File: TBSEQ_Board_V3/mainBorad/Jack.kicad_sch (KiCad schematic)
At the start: 7 parts

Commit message: BoardV3
ERCチェック済
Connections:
- net D+PlugIn_SyncIn: no longer names the net of DgJ9.4 (3)
- no-connect marks 3 -> 4
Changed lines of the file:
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@@
 		(at 97.79 66.04)
 	)
-	(wire
-		(pts
-			(xy 92.71 124.46) (xy 92.71 118.11)
-		)
-		(stroke
-			(width 0)
-			(type default)
-		)
+	(no_connect
+		(at 96.52 118.11)
 	)
 	(wire
@@
 		(pts
 			(xy 128.27 118.11) (xy 119.38 118.11)
-		)
-		(stroke
-			(width 0)
-			(type default)
-		)
-	)
-	(wire
-		(pts
-			(xy 96.52 124.46) (xy 92.71 124.46)
-		)
-		(stroke
-			(width 0)
-			(type default)
-		)
-	)
-	(wire
-		(pts
-			(xy 92.71 118.11) (xy 96.52 118.11)
 		)
 		(stroke
@@
 				(hide yes)
 			)
-		)
-	)
-	(global_label "D+PlugIn_SyncIn"
-		(shape output)
-		(at 96.52 124.46 0)
-		(fields_autoplaced yes)
-		(effects
-			(font
-				(size 1.27 1.27)
-			)
-			(justify left)
-		)
-		(property "Intersheetrefs" "${INTERSHEET_REFS}"
-			(at 115.4707 124.46 0)
-			(effects
-				(font
-					(size 1.27 1.27)
-				)
-				(justify left)
-				(hide yes)
-			)

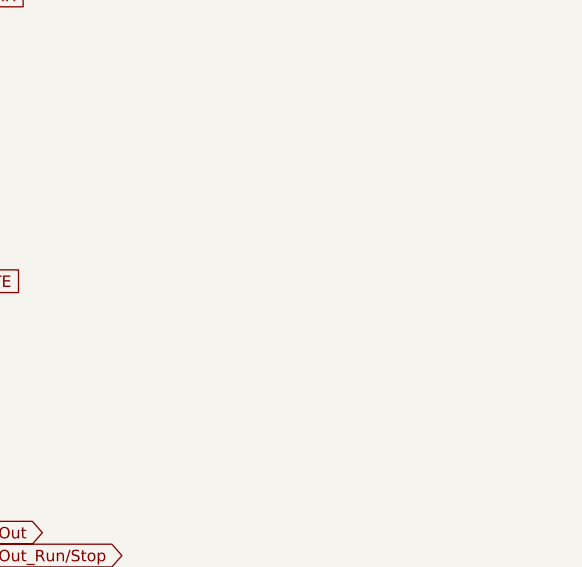
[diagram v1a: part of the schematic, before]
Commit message: V3Board
DualTr フットプリント変更
配線ミス修正
TEMPO削除⇒PanelBoardに移動
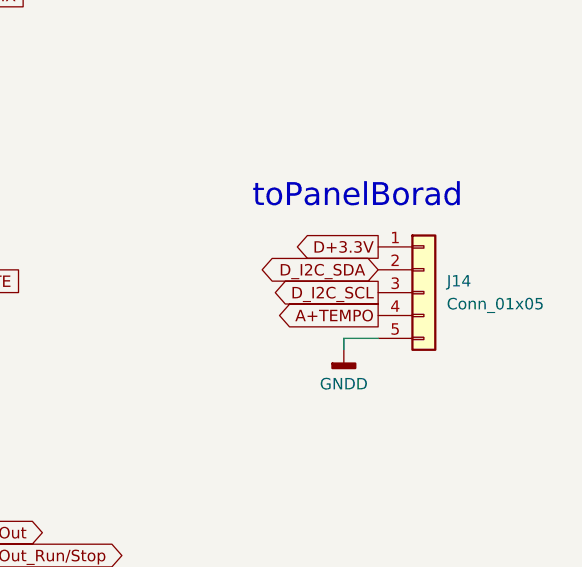
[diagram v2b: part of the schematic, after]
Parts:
- added J14: Conn_01x05, Connector_JST:JST_XH_S5B-XH-A-1_1x05_P2.50mm_Horizontal, symbol Connector_Generic:Conn_01x05
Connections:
- net D+3.3V: now also J14.1 (Pin_1)
- net GNDD: now also J14.5 (Pin_5)
- new net A+TEMPO: J14.4 (Pin_4)
- new net D_I2C_SCL: J14.3 (Pin_3)
- new net D_I2C_SDA: J14.2 (Pin_2)
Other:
- note added: "toPanelBorad"

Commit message: V3Board
アートワーク中
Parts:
- DgJ11: value MJ-8435 -> MJ-8435 CV OUT
- DgJ12: value MJ-8435 -> MJ-8435 GATE OUT
- DgJ13: value MJ-8435 -> MJ-8435 SYNC OUT
- DgJ9: value MJ-8435 -> MJ-8435 SYNC IN
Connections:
- net A+TEMPO: no longer names the net of J14.4 (Pin_4)
- no-connect marks 4 -> 5
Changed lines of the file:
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@@
+	)
+	(no_connect
+		(at 176.53 67.31)
 	)
 	(no_connect
@@
 				)
 				(justify left)
-				(hide yes)
-			)
-		)
-	)
-	(global_label "A+TEMPO"
-		(shape output)
-		(at 176.53 67.31 180)
-		(fields_autoplaced yes)
-		(effects
-			(font
-				(size 1.27 1.27)
-			)
-			(justify right)
-		)
-		(property "Intersheetrefs" "${INTERSHEET_REFS}"
-			(at 164.7153 67.31 0)
-			(effects
-				(font
-					(size 1.27 1.27)
-				)
-				(justify right)
 				(hide yes)
 			)
@@
 			)
 		)
+		(property "Sim.Library" ""
+			(at 140.97 143.51 0)
+			(effects
+				(font
+					(size 1.27 1.27)
+				)
+				(hide yes)
+			)
+		)
+		(property "Sim.Name" ""
+			(at 140.97 143.51 0)
+			(effects
+				(font
+					(size 1.27 1.27)
+				)
+				(hide yes)
+			)
+		)
 		(pin "2"
 		)
@@
 			)
 		)
-		(property "Value" "MJ-8435"
+		(property "Value" "MJ-8435 SYNC OUT"
 			(at 109.22 86.36 0)
 			(effects
@@
 				)
 				(justify left top)
+				(hide yes)
+			)
+		)
+		(property "Sim.Library" ""
+			(at 97.79 91.44 0)
+			(effects
+				(font
+					(size 1.27 1.27)
+				)
+				(hide yes)
+			)
+		)
+		(property "Sim.Name" ""
+			(at 97.79 91.44 0)
+			(effects
+				(font
+					(size 1.27 1.27)
+				)
 				(hide yes)
 			)
@@
 			)
 		)
+		(property "Sim.Library" ""
+			(at 171.45 143.51 0)
+			(effects
+				(font
+					(size 1.27 1.27)
+				)
+				(hide yes)
+			)
+		)
+		(property "Sim.Name" ""
+			(at 171.45 143.51 0)
+			(effects
+				(font
+					(size 1.27 1.27)
+				)
+				(hide yes)
+			)
+		)
 		(pin "2"
 		)
@@
 			)
 		)
-		(property "Value" "MJ-8435"
+		(property "Value" "MJ-8435 SYNC IN"
 			(at 107.95 110.49 0)
 			(effects
@@
 				)
 				(justify left top)
+				(hide yes)
+			)
+		)
+		(property "Sim.Library" ""
+			(at 96.52 115.57 0)
+			(effects
+				(font
+					(size 1.27 1.27)
+				)
+				(hide yes)
+			)
+		)
+		(property "Sim.Name" ""
+			(at 96.52 115.57 0)
+			(effects
+				(font
+					(size 1.27 1.27)
+				)
 				(hide yes)
 			)
@@
 			)
 		)
+		(property "Sim.Library" ""
+			(at 109.22 146.05 0)
+			(effects
+				(font
+					(size 1.27 1.27)
+				)
+				(hide yes)
+			)
+		)
+		(property "Sim.Name" ""
+			(at 109.22 146.05 0)
+			(effects
+				(font
+					(size 1.27 1.27)
+				)
+				(hide yes)
+			)
+		)
 		(pin "3"
 		)
@@
 			)
 		)
-		(property "Value" "MJ-8435"
+		(property "Value" "MJ-8435 CV OUT"
 			(at 109.22 26.67 0)
 			(effects
@@
 				)
 				(justify left top)
+				(hide yes)
+			)
+		)
+		(property "Sim.Library" ""
+			(at 97.79 31.75 0)
+			(effects
+				(font
+					(size 1.27 1.27)
+				)
+				(hide yes)
+			)
+		)
+		(property "Sim.Name" ""
+			(at 97.79 31.75 0)
+			(effects
+				(font
+					(size 1.27 1.27)
+				)
 				(hide yes)
 			)
@@
 			)
 		)
+		(property "Sim.Library" ""
+			(at 181.61 64.77 0)
+			(effects
+				(font
+					(size 1.27 1.27)
+				)
+				(hide yes)
+			)
+		)
+		(property "Sim.Name" ""
+			(at 181.61 64.77 0)
+			(effects
+				(font
+					(size 1.27 1.27)
+				)
+				(hide yes)
+			)
+		)
 		(pin "1"
 		)
@@
 			)
 		)
-		(property "Value" "MJ-8435"
+		(property "Value" "MJ-8435 GATE OUT"
 			(at 109.22 58.42 0)
 			(effects
@@
 				(hide yes)
 			)
+		)
+		(property "Sim.Library" ""
+			(at 97.79 63.5 0)
+			(effects
+				(font
+					(size 1.27 1.27)
+				)
+				(hide yes)
+			)
+		)
+		(property "Sim.Name" ""
+			(at 97.79 63.5 0)
+			(effects
+				(font
+					(size 1.27 1.27)
+				)
+				(hide yes)
+			)

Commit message: V3Board
GNDパターン塗り済
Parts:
- J14: footprint Connector_JST:JST_XH_S5B-XH-A-1_1x05_P2.50mm_Horizontal -> Connector_JST:JST_XH_B5B-XH-A_1x05_P2.50mm_Vertical
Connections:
- net A+CV_MIX renamed A+VCO_CV
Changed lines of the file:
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@@
 		)
 	)
-	(global_label "A+CV_MIX"
+	(global_label "A+VCO_CV"
 		(shape output)
 		(at 104.14 143.51 180)
@@
 		)
 	)
-	(global_label "A+CV_MIX"
+	(global_label "A+VCO_CV"
 		(shape input)
 		(at 125.73 31.75 0)
@@
 			)
 		)
-		(property "Footprint" "Connector_JST:JST_XH_S5B-XH-A-1_1x05_P2.50mm_Horizontal"
+		(property "Footprint" "Connector_JST:JST_XH_B5B-XH-A_1x05_P2.50mm_Vertical"
 			(at 181.61 64.77 0)
 			(effects
